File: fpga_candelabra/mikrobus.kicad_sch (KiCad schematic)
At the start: 19 parts, among them J6 Conn_mikroBUS_Host_2x8, U23 LSF0108PW, U24 LSF0108PW

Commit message: fpga_candelabra: sch & layout v0.5, pass basic ERC & DRC
Signed-off-by: Yichuan Gao <gaoyichuan000@gmail.com>
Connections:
- net MBUS_LV_AN renamed MBUS.AN
- net MBUS_LV_CS renamed MBUS.CS
- net MBUS_LV_INT renamed MBUS.INT
- net MBUS_LV_MISO renamed MBUS.MISO
- net MBUS_LV_MOSI renamed MBUS.MOSI
- net MBUS_LV_PWM renamed MBUS.PWM
- net MBUS_LV_RST renamed MBUS.RST
- net MBUS_LV_RX renamed MBUS.RX
- net MBUS_LV_SCK renamed MBUS.SCK
- net MBUS_LV_SCL renamed MBUS.SCL
- net MBUS_LV_SDA renamed MBUS.SDA
- net MBUS_LV_TX renamed MBUS.TX
- no-connect marks 10 -> 12
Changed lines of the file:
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@@
 	(generator_version "8.0")
 	(paper "A4")
+	(bus_alias "MIKROBUS"
+		(members "MOSI" "MISO" "SCK" "CS" "RST" "AN" "PWM" "INT" "RX" "TX" "SCL"
+			"SDA"
+		)
+	)
 	(junction
 		(at 104.14 38.1)
@@
 	)
 	(no_connect
+		(at 124.46 138.43)
+	)
+	(no_connect
+		(at 121.92 138.43)
+	)
+	(no_connect
 		(at 121.92 49.53)
 	)
@@
 		)
 	)
+	(bus
+		(pts
+			(xy 247.65 160.02) (xy 267.97 160.02)
+		)
+		(stroke
+			(width 0)
+			(type default)
+		)
+	)
 	(wire
 		(pts
@@
 		)
 	)
-	(label "MBUS_LV_MISO"
+	(label "MBUS.MISO"
 		(at 29.21 57.15 0)
 		(fields_autoplaced yes)
@@
 		)
 	)
-	(label "MBUS_LV_CS"
+	(label "MBUS.CS"
 		(at 29.21 67.31 0)
 		(fields_autoplaced yes)
@@
 		)
 	)
-	(label "MBUS_LV_SCK"
+	(label "MBUS.SCK"
 		(at 29.21 62.23 0)
 		(fields_autoplaced yes)
@@
 		)
 	)
-	(label "MBUS_LV_SDA"
+	(label "MBUS.SDA"
 		(at 29.21 166.37 0)
 		(fields_autoplaced yes)
@@
 		)
 	)
-	(label "MBUS_LV_SCL"
+	(label "MBUS.SCL"
 		(at 29.21 161.29 0)
 		(fields_autoplaced yes)
@@
 		)
 	)
-	(label "MBUS_LV_RST"
+	(label "MBUS.RST"
 		(at 29.21 72.39 0)
 		(fields_autoplaced yes)
@@
 		)
 	)
-	(label "MBUS_LV_MOSI"
+	(label "MBUS.MOSI"
 		(at 29.21 52.07 0)
 		(fields_autoplaced yes)
@@
 		)
 	)
-	(label "MBUS_LV_PWM"
+	(label "MBUS.PWM"
 		(at 29.21 140.97 0)
 		(fields_autoplaced yes)
@@
 		)
 	)
-	(label "MBUS_LV_RX"
+	(label "MBUS.RX"
 		(at 29.21 151.13 0)
 		(fields_autoplaced yes)
@@
 		)
 	)
+	(label "MBUS{MIKROBUS}"
+		(at 248.92 160.02 0)
+		(fields_autoplaced yes)
+		(effects
+			(font
+				(size 1.27 1.27)
+			)
+			(justify left bottom)
+		)
+	)
 	(label "MBUS_HV_MOSI"
 		(at 184.15 55.88 0)
@@
 		)
 	)
-	(label "MBUS_LV_TX"
+	(label "MBUS.TX"
 		(at 29.21 156.21 0)
 		(fields_autoplaced yes)
@@
 		)
 	)
-	(label "MBUS_LV_AN"
+	(label "MBUS.AN"
 		(at 29.21 77.47 0)
 		(fields_autoplaced yes)
@@
 		)
 	)
-	(label "MBUS_LV_INT"
+	(label "MBUS.INT"
 		(at 29.21 146.05 0)
 		(fields_autoplaced yes)
@@
 		)
 	)
+	(hierarchical_label "MBUS{MIKROBUS}"
+		(shape bidirectional)
+		(at 247.65 160.02 180)
+		(fields_autoplaced yes)
+		(effects
+			(font
+				(size 1.27 1.27)
+			)
+			(justify right)
+		)
+	)
 	(symbol
 		(lib_id "power:Earth")
@@
 	)
 	(symbol
+		(lib_id "CHIPSAlliance_Power:PWR_FLAG")
+		(at 96.52 121.92 0)
+		(unit 1)
+		(exclude_from_sim no)
+		(in_bom yes)
+		(on_board yes)
+		(dnp no)
+		(fields_autoplaced yes)
+		(property "Reference" "#FLG029"
+			(at 96.52 120.015 0)
+			(effects
+				(font
+					(size 1.27 1.27)
+				)
+				(hide yes)
+			)
+		)
+		(property "Value" "PWR_FLAG"
+			(at 96.52 117.7869 0)
+			(effects
+				(font
+					(size 1.27 1.27)
+				)
+				(hide yes)
+			)
+		)
+		(property "Footprint" ""
+			(at 96.52 121.92 0)
+			(effects
+				(font
+					(size 1.27 1.27)
+				)
+				(hide yes)
+			)
+		)
+		(property "Datasheet" "~"
+			(at 96.52 121.92 0)
+			(effects
+				(font
+					(size 1.27 1.27)
+				)
+				(hide yes)
+			)
+		)
+		(property "Description" "Special symbol for telling ERC where power comes from"
+			(at 96.52 121.92 0)
+			(effects
+				(font
+					(size 1.27 1.27)
+				)
+				(hide yes)
+			)
+		)
+		(pin "1"
+		)
+		(instances
+			(project "fpga_candelabra"
+				(path "/01ed9e92-4e50-4b41-90dc-10444aaec5f7/4a6f2e76-d40d-4b0b-994b-17cbcb86cc6a"
+					(reference "#FLG029")
+					(unit 1)
+				)
+			)
+		)
+	)
+	(symbol
 		(lib_id "power:+1V8")
 		(at 60.96 125.73 0)
@@
 					(unit 1)
 				)
+			)
+		)
+	)
+	(symbol
+		(lib_id "CHIPSAlliance_Power:PWR_FLAG")
+		(at 96.52 33.02 0)
+		(unit 1)
+		(exclude_from_sim no)
+		(in_bom yes)
+		(on_board yes)
+		(dnp no)
+		(fields_autoplaced yes)
+		(property "Reference" "#FLG04"
+			(at 96.52 31.115 0)
+			(effects
+				(font
+					(size 1.27 1.27)
+				)
+				(hide yes)
+			)
+		)
+		(property "Value" "PWR_FLAG"
+			(at 96.52 28.8869 0)
+			(effects
+				(font
+					(size 1.27 1.27)
+				)
+				(hide yes)
+			)
+		)
+		(property "Footprint" ""
+			(at 96.52 33.02 0)
+			(effects
+				(font
+					(size 1.27 1.27)
+				)
+				(hide yes)
+			)
+		)
+		(property "Datasheet" "~"
+			(at 96.52 33.02 0)
+			(effects
+				(font
+					(size 1.27 1.27)
+				)
+				(hide yes)
+			)
+		)
+		(property "Description" "Special symbol for telling ERC where power comes from"
+			(at 96.52 33.02 0)
+			(effects
+				(font
+					(size 1.27 1.27)
+				)
+				(hide yes)
+			)
+		)
+		(pin "1"
+		)
+		(instances
+			(project "fpga_candelabra"
+				(path "/01ed9e92-4e50-4b41-90dc-10444aaec5f7/4a6f2e76-d40d-4b0b-994b-17cbcb86cc6a"
+					(reference "#FLG04")
+					(unit 1)
+				)

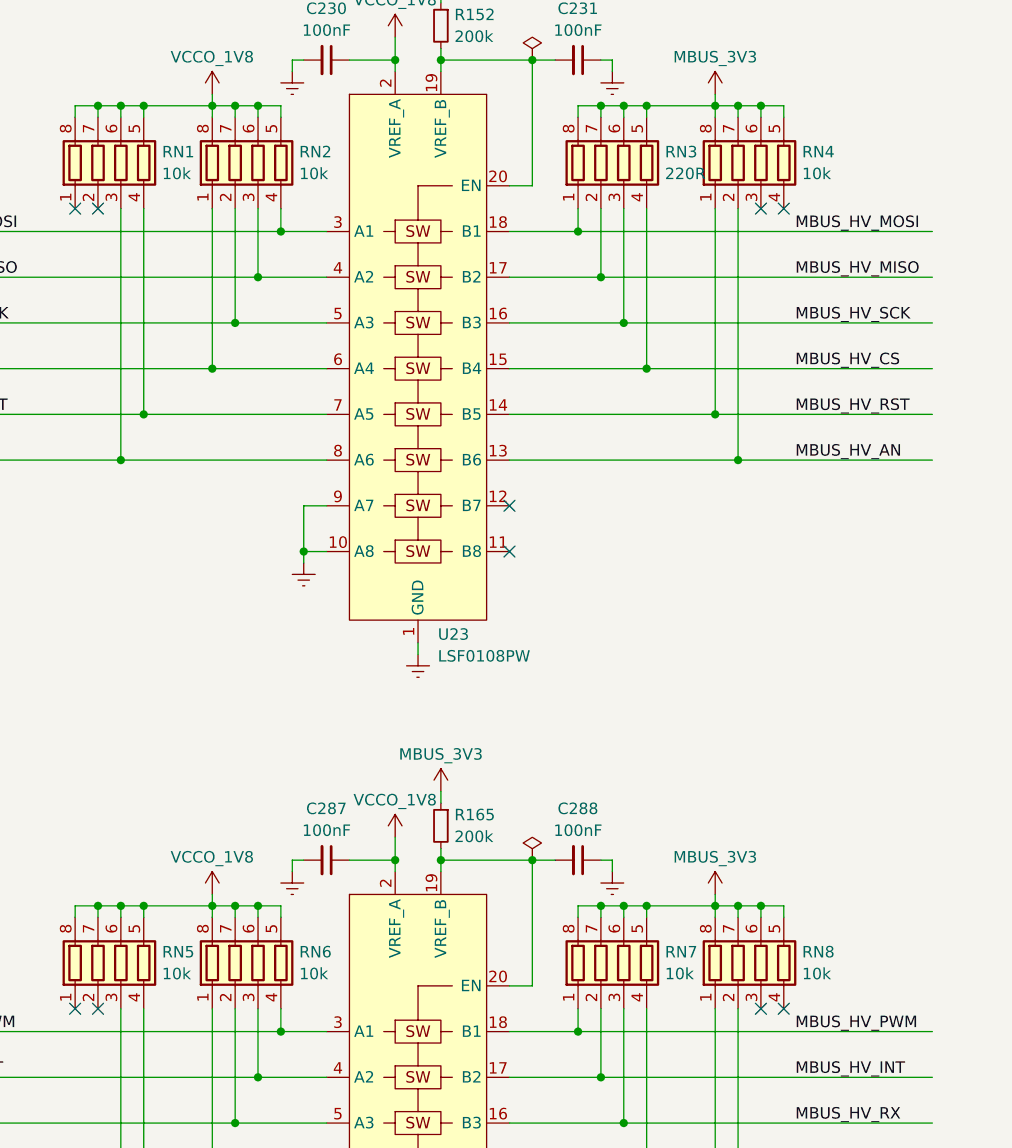
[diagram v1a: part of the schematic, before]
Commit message: fpga_candelabra: more bugfixes & improvements for rev 0.2.0
- Add Digilent JTAG-SMT2-NC onboard
- Add fan controller & 4pin fan header
- Use 9pin header for USB2.0
- Misc fixes for structure

Signed-off-by: Yichuan Gao <gaoyichuan000@gmail.com>
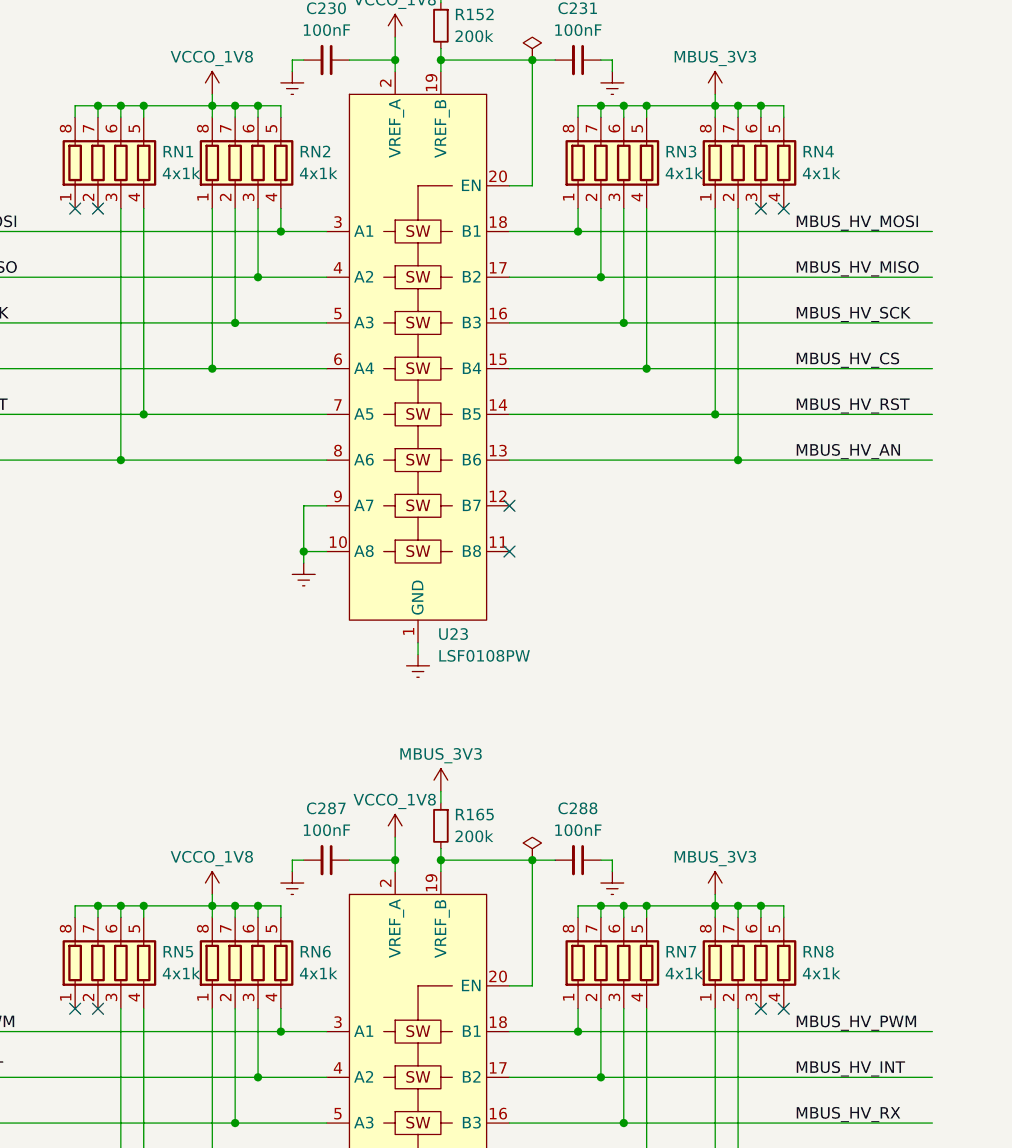
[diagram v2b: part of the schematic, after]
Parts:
- RN1, RN2, RN4, RN5, RN6, RN7, RN8: value 10k -> 4x1k
- RN3: value 220R -> 4x1k
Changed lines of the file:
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@@
 	(generator_version "8.0")
 	(paper "A4")
-	(bus_alias "MIKROBUS"
-		(members "MOSI" "MISO" "SCK" "CS" "RST" "AN" "PWM" "INT" "RX" "TX" "SCL"
-			"SDA"
-		)
-	)
 	(junction
 		(at 104.14 38.1)
@@
 	(label "MBUS_HV_MISO"
 		(at 184.15 53.34 0)
-		(fields_autoplaced yes)
 		(effects
 			(font
@@
 	(label "MBUS_HV_INT"
 		(at 125.73 146.05 0)
-		(fields_autoplaced yes)
 		(effects
 			(font
@@
 	(label "MBUS_HV_INT"
 		(at 220.98 45.72 0)
-		(fields_autoplaced yes)
 		(effects
 			(font
@@
 	(label "MBUS.MISO"
 		(at 29.21 57.15 0)
-		(fields_autoplaced yes)
 		(effects
 			(font
@@
 	(label "MBUS.CS"
 		(at 29.21 67.31 0)
-		(fields_autoplaced yes)
 		(effects
 			(font
@@
 	(label "MBUS_HV_RX"
 		(at 125.73 151.13 0)
-		(fields_autoplaced yes)
 		(effects
 			(font
@@
 	(label "MBUS_HV_CS"
 		(at 125.73 67.31 0)
-		(fields_autoplaced yes)
 		(effects
 			(font
@@
 	(label "MBUS_HV_MISO"
 		(at 125.73 57.15 0)
-		(fields_autoplaced yes)
 		(effects
 			(font
@@
 	(label "MBUS_HV_SCK"
 		(at 125.73 62.23 0)
-		(fields_autoplaced yes)
 		(effects
 			(font
@@
 	(label "MBUS.SCK"
 		(at 29.21 62.23 0)
-		(fields_autoplaced yes)
 		(effects
 			(font
@@
 	(label "MBUS_HV_SDA"
 		(at 220.98 55.88 0)
-		(fields_autoplaced yes)
 		(effects
 			(font
@@
 	(label "MBUS_HV_AN"
 		(at 125.73 77.47 0)
-		(fields_autoplaced yes)
 		(effects
 			(font
@@
 	(label "MBUS_HV_CS"
 		(at 184.15 48.26 0)
-		(fields_autoplaced yes)
 		(effects
 			(font
@@
 	(label "MBUS.SDA"
 		(at 29.21 166.37 0)
-		(fields_autoplaced yes)
 		(effects
 			(font
@@
 	(label "MBUS_HV_SCK"
 		(at 184.15 50.8 0)
-		(fields_autoplaced yes)
 		(effects
 			(font
@@
 	(label "MBUS_HV_MOSI"
 		(at 125.73 52.07 0)
-		(fields_autoplaced yes)
 		(effects
 			(font
@@
 	(label "MBUS.SCL"
 		(at 29.21 161.29 0)
-		(fields_autoplaced yes)
 		(effects
 			(font
@@
 	(label "MBUS_HV_TX"
 		(at 125.73 156.21 0)
-		(fields_autoplaced yes)
 		(effects
 			(font
@@
 	(label "MBUS_HV_RST"
 		(at 184.15 45.72 0)
-		(fields_autoplaced yes)
 		(effects
 			(font
@@
 	(label "MBUS_HV_PWM"
 		(at 220.98 43.18 0)
-		(fields_autoplaced yes)
 		(effects
 			(font
@@
 	(label "MBUS_HV_TX"
 		(at 220.98 50.8 0)
-		(fields_autoplaced yes)
 		(effects
 			(font
@@
 	(label "MBUS_HV_RST"
 		(at 125.73 72.39 0)
-		(fields_autoplaced yes)
 		(effects
 			(font
@@
 	(label "MBUS.RST"
 		(at 29.21 72.39 0)
-		(fields_autoplaced yes)
 		(effects
 			(font
@@
 	(label "MBUS.MOSI"
 		(at 29.21 52.07 0)
-		(fields_autoplaced yes)
 		(effects
 			(font
@@
 	(label "MBUS_HV_SDA"
 		(at 125.73 166.37 0)
-		(fields_autoplaced yes)
 		(effects
 			(font
@@
 	(label "MBUS_HV_PWM"
 		(at 125.73 140.97 0)
-		(fields_autoplaced yes)
 		(effects
 			(font
@@
 	(label "MBUS_HV_RX"
 		(at 220.98 48.26 0)
-		(fields_autoplaced yes)
 		(effects
 			(font
@@
 	(label "MBUS_HV_SCL"
 		(at 220.98 53.34 0)
-		(fields_autoplaced yes)
 		(effects
 			(font
@@
 	(label "MBUS.PWM"
 		(at 29.21 140.97 0)
-		(fields_autoplaced yes)
 		(effects
 			(font
@@
 	(label "MBUS.RX"
 		(at 29.21 151.13 0)
-		(fields_autoplaced yes)
 		(effects
 			(font
@@
 	(label "MBUS{MIKROBUS}"
 		(at 248.92 160.02 0)
-		(fields_autoplaced yes)
 		(effects
 			(font
@@
 	(label "MBUS_HV_MOSI"
 		(at 184.15 55.88 0)
-		(fields_autoplaced yes)
 		(effects
 			(font
@@
 	(label "MBUS.TX"
 		(at 29.21 156.21 0)
-		(fields_autoplaced yes)
 		(effects
 			(font
@@
 	(label "MBUS.AN"
 		(at 29.21 77.47 0)
-		(fields_autoplaced yes)
 		(effects
 			(font
@@
 	(label "MBUS_HV_SCL"
 		(at 125.73 161.29 0)
-		(fields_autoplaced yes)
 		(effects
 			(font
@@
 	(label "MBUS.INT"
 		(at 29.21 146.05 0)
-		(fields_autoplaced yes)
 		(effects
 			(font
@@
 	(label "MBUS_HV_AN"
 		(at 184.15 43.18 0)
-		(fields_autoplaced yes)
 		(effects
 			(font
@@
 		(shape bidirectional)
 		(at 247.65 160.02 180)
-		(fields_autoplaced yes)
 		(effects
 			(font
@@
 			)
 		)
-		(property "Value" "10k"
+		(property "Value" "4x1k"
 			(at 126.492 134.5621 0)
 			(effects
@@
 			)
 		)
-		(property "Value" "10k"
+		(property "Value" "4x1k"
 			(at 55.372 45.6621 0)
 			(effects
@@
 			)
 		)
-		(property "Value" "10k"
+		(property "Value" "4x1k"
 			(at 126.492 45.6621 0)
 			(effects
@@
 			)
 		)
-		(property "Value" "220R"
+		(property "Value" "4x1k"
 			(at 111.252 45.6621 0)
 			(effects
@@
 			)
 		)
-		(property "Value" "10k"
+		(property "Value" "4x1k"
 			(at 70.612 134.5621 0)
 			(effects
@@
 			)
 		)
-		(property "Value" "10k"
+		(property "Value" "4x1k"
 			(at 55.372 134.5621 0)
 			(effects
@@
 			)
 		)
-		(property "Value" "10k"
+		(property "Value" "4x1k"
 			(at 70.612 45.6621 0)
 			(effects
@@
 			)
 		)
-		(property "Value" "10k"
+		(property "Value" "4x1k"
 			(at 111.252 134.5621 0)
 			(effects

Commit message: fpga_candelabra: add author & rev to schematics
Signed-off-by: Yichuan Gao <gaoyichuan000@gmail.com>
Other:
- company: (none) -> CHIPS Alliance
- title: (none) -> mikroBUS Connector
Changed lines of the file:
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@@
 	(generator_version "8.0")
 	(paper "A4")
+	(title_block
+		(title "mikroBUS Connector")
+		(date "2025-02-05")
+		(rev "0.2.0")
+		(company "CHIPS Alliance")
+		(comment 1 "Yichuan Gao")
+		(comment 2 "Yichuan Gao")
+	)
 	(junction
 		(at 104.14 38.1)

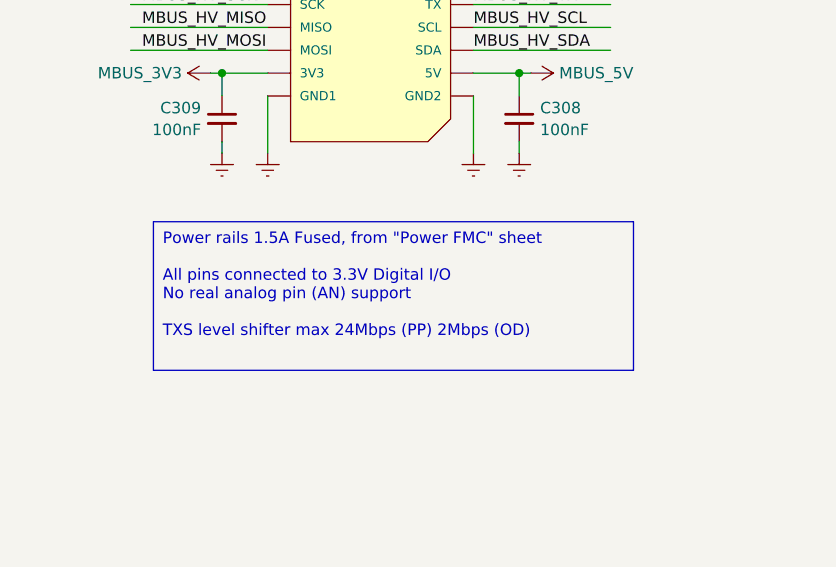
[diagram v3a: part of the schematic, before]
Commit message: fpga_candelabra: update to kicad 9.0
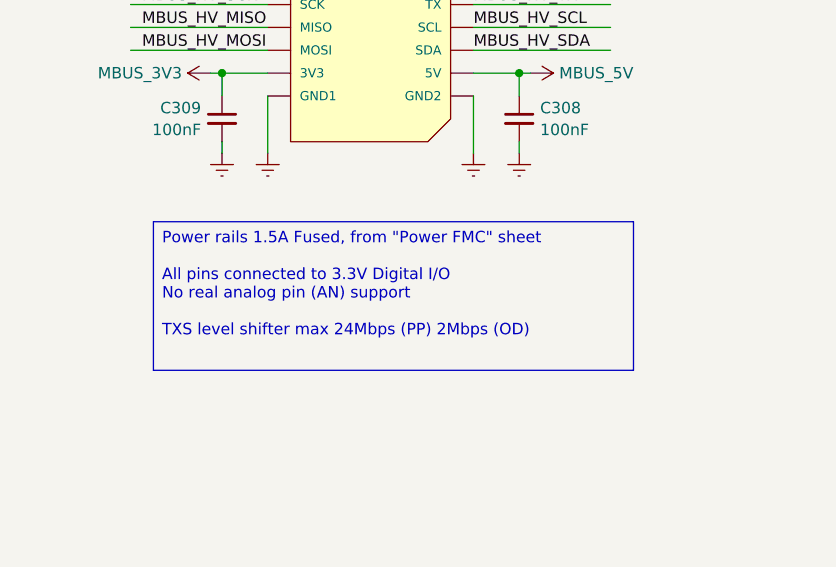
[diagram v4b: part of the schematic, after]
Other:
- company: CHIPS Alliance -> Sipeed
